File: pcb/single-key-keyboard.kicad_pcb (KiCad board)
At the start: 2 copper layers, 30.1 x 57.6 mm, 30 parts, among them J2 Conn_01x05, P1 USB_C_Plug_USB2.0, SW1 SW_Push, SW2 SW_SPST, U1 ATtiny416-M

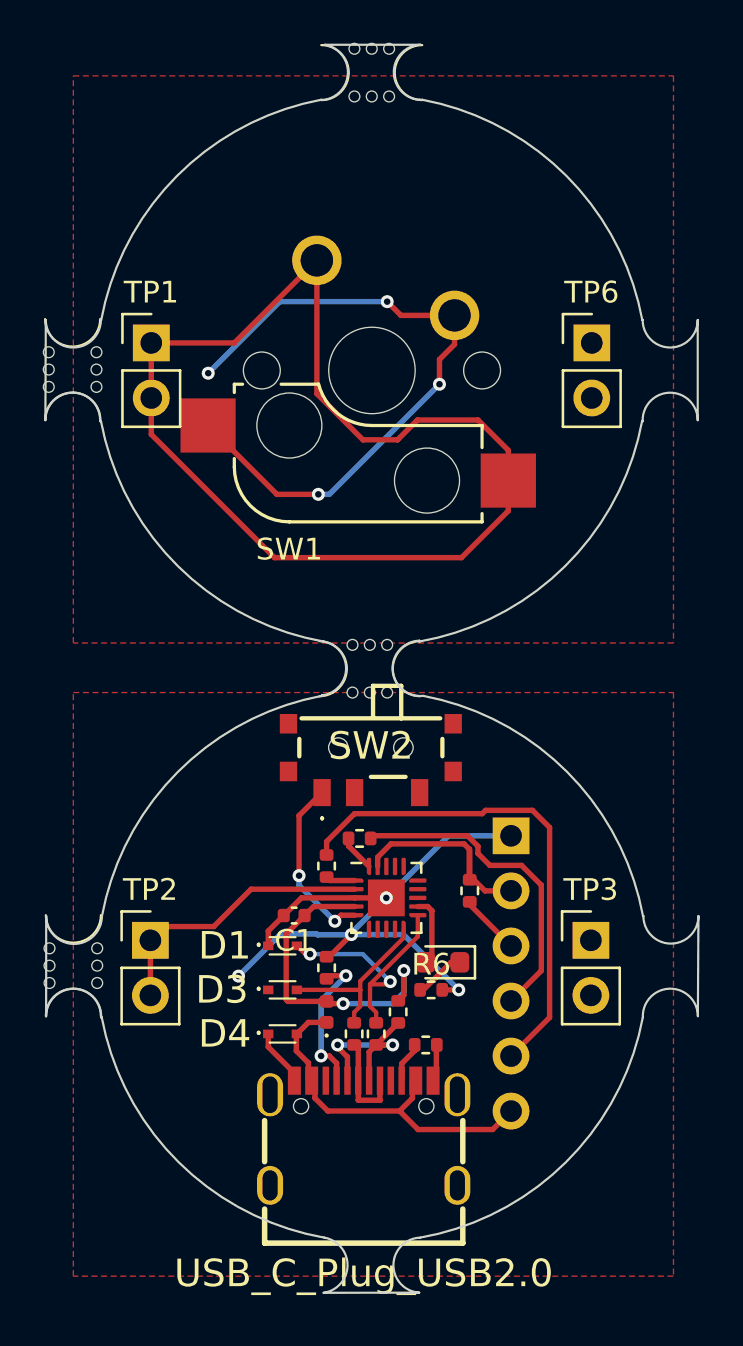
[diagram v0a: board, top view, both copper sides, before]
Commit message: Code compiles and pick correct pcb version
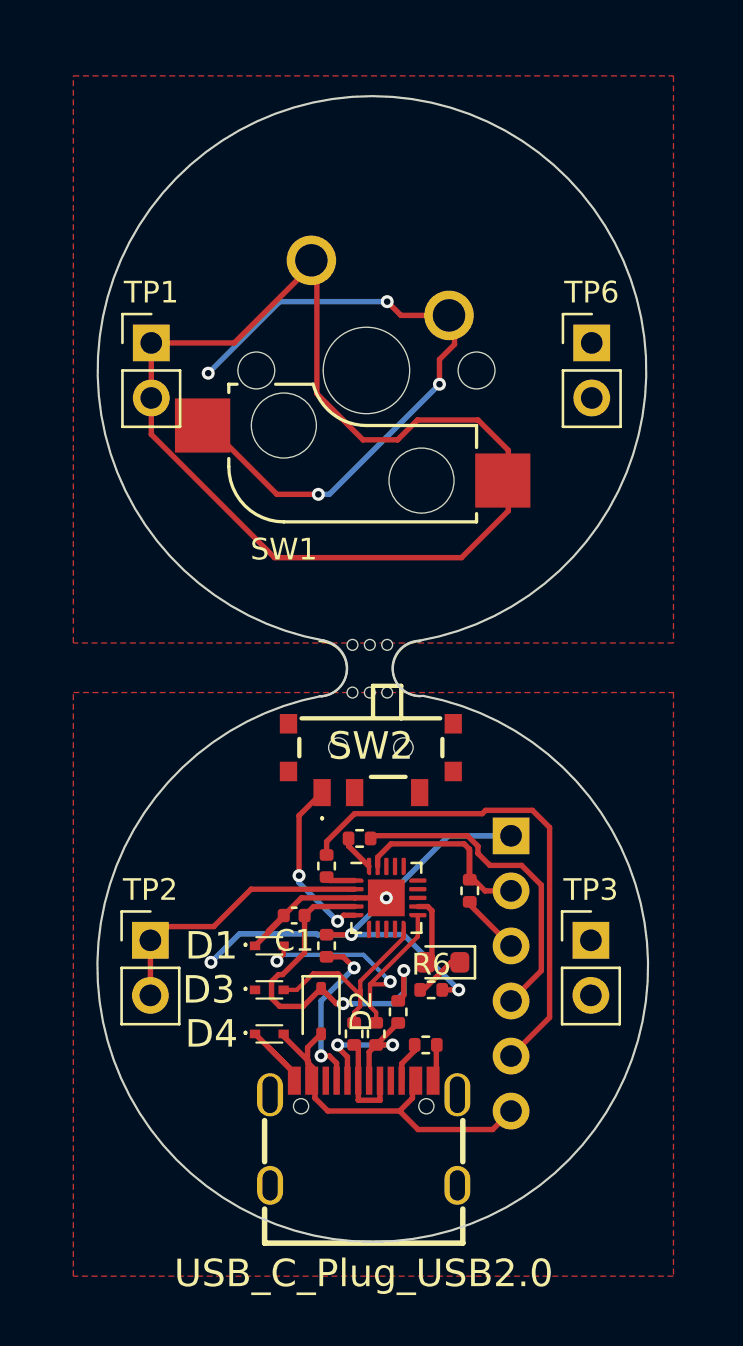
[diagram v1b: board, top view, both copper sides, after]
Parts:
- removed H3 (x2), H4: MountingHole, panelization:mouse-bite-2.54mm-slot
- removed REF**: NkJcm501, walking-boat:test
- D2: footprint Diode_SMD:D_0402_1005Metric -> Diode_SMD:D_SOD-323
- moved R2 1.02 mm to (138.9, 124.7)
- moved D1 0.61 mm to (136.3, 124.7)
- moved D3 0.61 mm to (136.3, 126.7)
- moved D4 0.61 mm to (136.3, 128.8)
- moved D2 0.26 mm to (138.7, 127.7), turned to -90 degrees
- moved SW1 0.25 mm to (140.8, 98.2)
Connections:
- D2 pad 1: /VIN -> +5VP
- D2 pad 2: +5VP -> /VIN
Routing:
- net GND: track 35.1 -> 39.3 mm
- net /VIN: track 16.4 -> 18.5 mm
- net +5VP: track 15.0 -> 16.7 mm
- net /D-: track 12.0 -> 13.7 mm
- net /D+: track 8.19 -> 9.79 mm
- net Net-(P1-CC1): track 6.79 -> 7.84 mm
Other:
- board size 30.1 x 57.6 mm -> 25.4 x 52.9 mm
